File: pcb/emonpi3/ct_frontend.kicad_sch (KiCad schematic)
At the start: 9 parts, among them J1 SJ-3524-SMT-TR

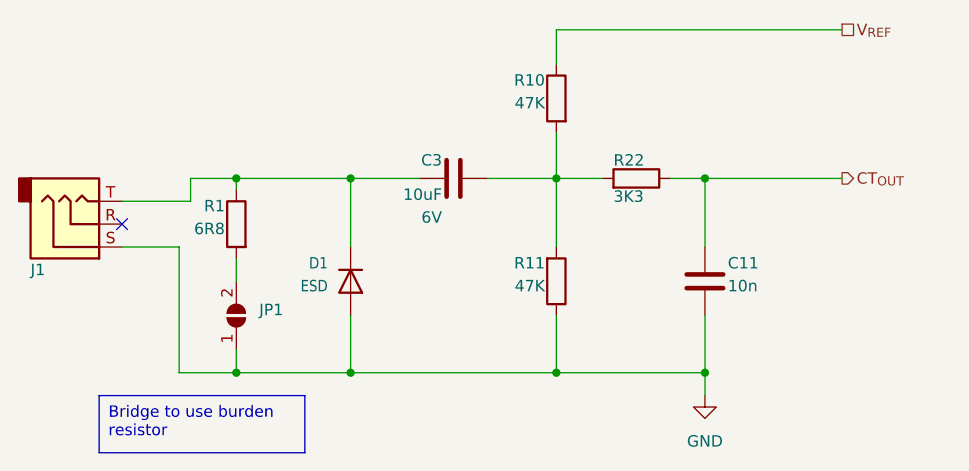
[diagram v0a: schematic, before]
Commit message: * [ESD] Revise ESD protection strategy
  - All inputs and buttons have TVS and injection current limit
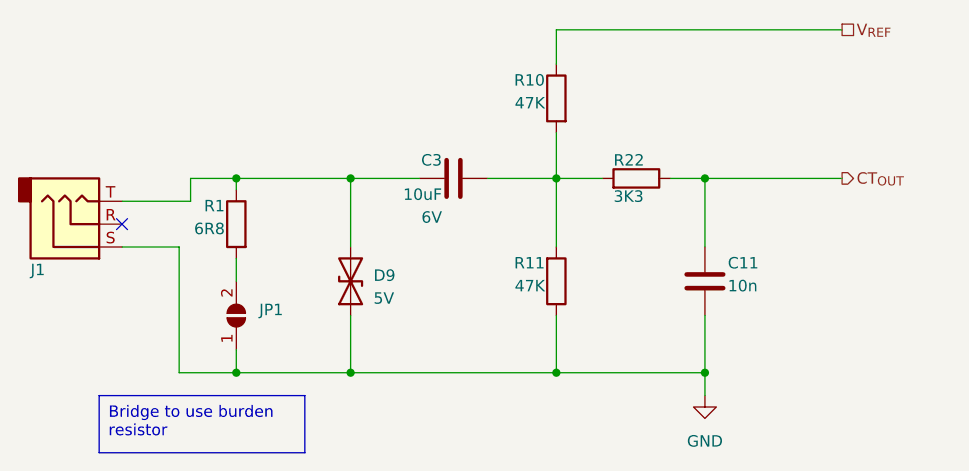
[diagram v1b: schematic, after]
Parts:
- removed D1: ESD, Diode_SMD:D_SOD-523, symbol Device:D
- added D9: 5V, Diode_SMD:D_SOD-523, symbol Device:D_TVS
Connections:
- net GND: now also D9.1 (A1)
- net at C3.1, J1.T, R1.1: now also D9.2 (A2)
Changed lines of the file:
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@@
     )
   )
-  (symbol (lib_id "Device:D") (at 128.27 96.52 270) (unit 1)
-    (in_bom yes) (on_board yes) (dnp no)
-    (property "Reference" "D1" (at 125.73 95.25 90)
-      (effects (font (size 1.27 1.0795)) (justify right bottom))
+  (symbol (lib_id "Device:D_TVS") (at 128.27 96.52 90) (unit 1)
+    (in_bom yes) (on_board yes) (dnp no) (fields_autoplaced)
+    (property "Reference" "D9" (at 130.81 95.885 90)
+      (effects (font (size 1.27 1.27)) (justify right))
     )
-    (property "Value" "ESD" (at 125.73 97.79 90)
-      (effects (font (size 1.27 1.0795)) (justify right bottom))
+    (property "Value" "5V" (at 130.81 98.425 90)
+      (effects (font (size 1.27 1.27)) (justify right))
     )
     (property "Footprint" "Diode_SMD:D_SOD-523" (at 128.27 96.52 0)
       (effects (font (size 1.27 1.27)) hide)
     )
-    (property "Datasheet" "~" (at 128.27 96.52 0)
+    (property "Datasheet" "https://www.mouser.co.uk/datasheet/2/408/DF2B7AE_datasheet_en_20220907-1128333.pdf" (at 128.27 96.52 0)
       (effects (font (size 1.27 1.27)) hide)
     )
-    (property "Sim.Device" "D" (at 128.27 96.52 0)
+    (property "Manufacturer" "Toshiba" (at 128.27 96.52 90)
       (effects (font (size 1.27 1.27)) hide)
     )
-    (property "Sim.Pins" "1=K 2=A" (at 128.27 96.52 0)
+    (property "MPN" "DF2B7AE,H3F" (at 128.27 96.52 90)
+      (effects (font (size 1.27 1.27)) hide)
+    )
+    (property "Mouser" "757-DF2B7AEH3F" (at 128.27 96.52 90)
       (effects (font (size 1.27 1.27)) hide)
     )
@@
       (project "emonPi3"
         (path "/3a5f1087-1abe-4575-9313-bd86a5e03366"
-          (reference "D1") (unit 1)
+          (reference "D9") (unit 1)
         )
         (path "/3a5f1087-1abe-4575-9313-bd86a5e03366/d70e4664-3b09-489f-91b5-f7b96a995bad"
@@
           (reference "D2") (unit 1)
         )
+        (path "/3a5f1087-1abe-4575-9313-bd86a5e03366/8a757211-ae24-4f4a-9f79-317e71cc2f8d"
+          (reference "D3") (unit 1)
+        )
         (path "/3a5f1087-1abe-4575-9313-bd86a5e03366/243cba72-07dc-4281-adcf-99d985c9a58a"
           (reference "D4") (unit 1)
         )
-        (path "/3a5f1087-1abe-4575-9313-bd86a5e03366/8a757211-ae24-4f4a-9f79-317e71cc2f8d"
-          (reference "D3") (unit 1)
-        )
         (path "/3a5f1087-1abe-4575-9313-bd86a5e03366/67ec4105-ad3e-41cc-8c86-c0216f06fea4"

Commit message: * [v0.2] Final touches for manufacture
  - Remove h/w zero crossing
  - Adjust hole spacing for CT expander
  - Add teardrops
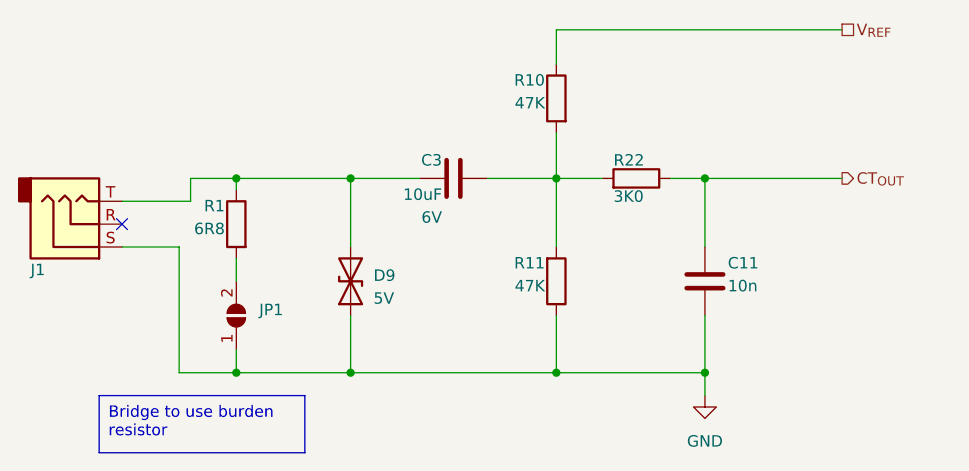
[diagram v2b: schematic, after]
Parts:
- R22: value 3K3 -> 3K0
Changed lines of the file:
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@@
       (effects (font (size 1.27 1.27)) (justify left top))
     )
-    (property "Value" "3K3" (at 157.48 86.36 90)
+    (property "Value" "3K0" (at 157.48 86.36 90)
       (effects (font (size 1.27 1.27)) (justify left bottom))
     )

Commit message: Freeze for v1.0
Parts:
- renumbered D9 to D1
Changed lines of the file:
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@@
   (title_block
     (title "emonPi3")
-    (date "2024-12-28")
+    (date "2025-05-18")
     (rev "v1.0")
     (company "OpenEnergyMonitor / Tilt Ltd (Angus Logan)")
@@
     (instances
       (project "emonPi3"
-        (path "/3a5f1087-1abe-4575-9313-bd86a5e03366"
-          (reference "J1") (unit 1)
-        )
         (path "/3a5f1087-1abe-4575-9313-bd86a5e03366/d70e4664-3b09-489f-91b5-f7b96a995bad"
           (reference "J1") (unit 1)
@@
     (instances
       (project "emonPi3"
-        (path "/3a5f1087-1abe-4575-9313-bd86a5e03366"
-          (reference "R22") (unit 1)
-        )
         (path "/3a5f1087-1abe-4575-9313-bd86a5e03366/d70e4664-3b09-489f-91b5-f7b96a995bad"
           (reference "R22") (unit 1)
@@
     (instances
       (project "emonPi3"
-        (path "/3a5f1087-1abe-4575-9313-bd86a5e03366"
+        (path "/3a5f1087-1abe-4575-9313-bd86a5e03366/d70e4664-3b09-489f-91b5-f7b96a995bad"
           (reference "#PWR07") (unit 1)
         )
-        (path "/3a5f1087-1abe-4575-9313-bd86a5e03366/d70e4664-3b09-489f-91b5-f7b96a995bad"
-          (reference "#PWR07") (unit 1)
-        )
         (path "/3a5f1087-1abe-4575-9313-bd86a5e03366/0fb40f82-6e2c-4ad5-ba9c-527ae886c284"
           (reference "#PWR08") (unit 1)
@@
     (instances
       (project "emonPi3"
-        (path "/3a5f1087-1abe-4575-9313-bd86a5e03366"
-          (reference "R1") (unit 1)
-        )
         (path "/3a5f1087-1abe-4575-9313-bd86a5e03366/d70e4664-3b09-489f-91b5-f7b96a995bad"
           (reference "R1") (unit 1)
@@
   (symbol (lib_id "Device:D_TVS") (at 128.27 96.52 90) (unit 1)
     (in_bom yes) (on_board yes) (dnp no) (fields_autoplaced)
-    (property "Reference" "D9" (at 130.81 95.885 90)
+    (property "Reference" "D1" (at 130.81 95.885 90)
       (effects (font (size 1.27 1.27)) (justify right))
     )
@@
     (instances
       (project "emonPi3"
-        (path "/3a5f1087-1abe-4575-9313-bd86a5e03366"
-          (reference "D9") (unit 1)
-        )
         (path "/3a5f1087-1abe-4575-9313-bd86a5e03366/d70e4664-3b09-489f-91b5-f7b96a995bad"
           (reference "D1") (unit 1)
@@
     (instances
       (project "emonPi3"
-        (path "/3a5f1087-1abe-4575-9313-bd86a5e03366"
+        (path "/3a5f1087-1abe-4575-9313-bd86a5e03366/d70e4664-3b09-489f-91b5-f7b96a995bad"
           (reference "R10") (unit 1)
         )
-        (path "/3a5f1087-1abe-4575-9313-bd86a5e03366/d70e4664-3b09-489f-91b5-f7b96a995bad"
-          (reference "R10") (unit 1)
-        )
         (path "/3a5f1087-1abe-4575-9313-bd86a5e03366/0fb40f82-6e2c-4ad5-ba9c-527ae886c284"
           (reference "R3") (unit 1)
@@
     (instances
       (project "emonPi3"
-        (path "/3a5f1087-1abe-4575-9313-bd86a5e03366"
-          (reference "C11") (unit 1)
-        )
         (path "/3a5f1087-1abe-4575-9313-bd86a5e03366/d70e4664-3b09-489f-91b5-f7b96a995bad"
           (reference "C11") (unit 1)
@@
     (instances
       (project "emonPi3"
-        (path "/3a5f1087-1abe-4575-9313-bd86a5e03366"
-          (reference "R11") (unit 1)
-        )
         (path "/3a5f1087-1abe-4575-9313-bd86a5e03366/d70e4664-3b09-489f-91b5-f7b96a995bad"
           (reference "R11") (unit 1)
@@
     (instances
       (project "emonPi3"
-        (path "/3a5f1087-1abe-4575-9313-bd86a5e03366"
+        (path "/3a5f1087-1abe-4575-9313-bd86a5e03366/d70e4664-3b09-489f-91b5-f7b96a995bad"
           (reference "C3") (unit 1)
-        )
-        (path "/3a5f1087-1abe-4575-9313-bd86a5e03366/d70e4664-3b09-489f-91b5-f7b96a995bad"
-          (reference "C3") (unit 1)
